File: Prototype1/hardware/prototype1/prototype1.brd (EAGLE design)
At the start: 134.6 x 74.6 mm, 83 parts, among them IC1 ICE40UL1K-CM36AITR1K, IC2 LDL112D33R, IC3 FT2232HL-REEL, IC4 93LC46BT-I_OT, IC5 M95010-WMN6P, U2 ESP-WROOM-32

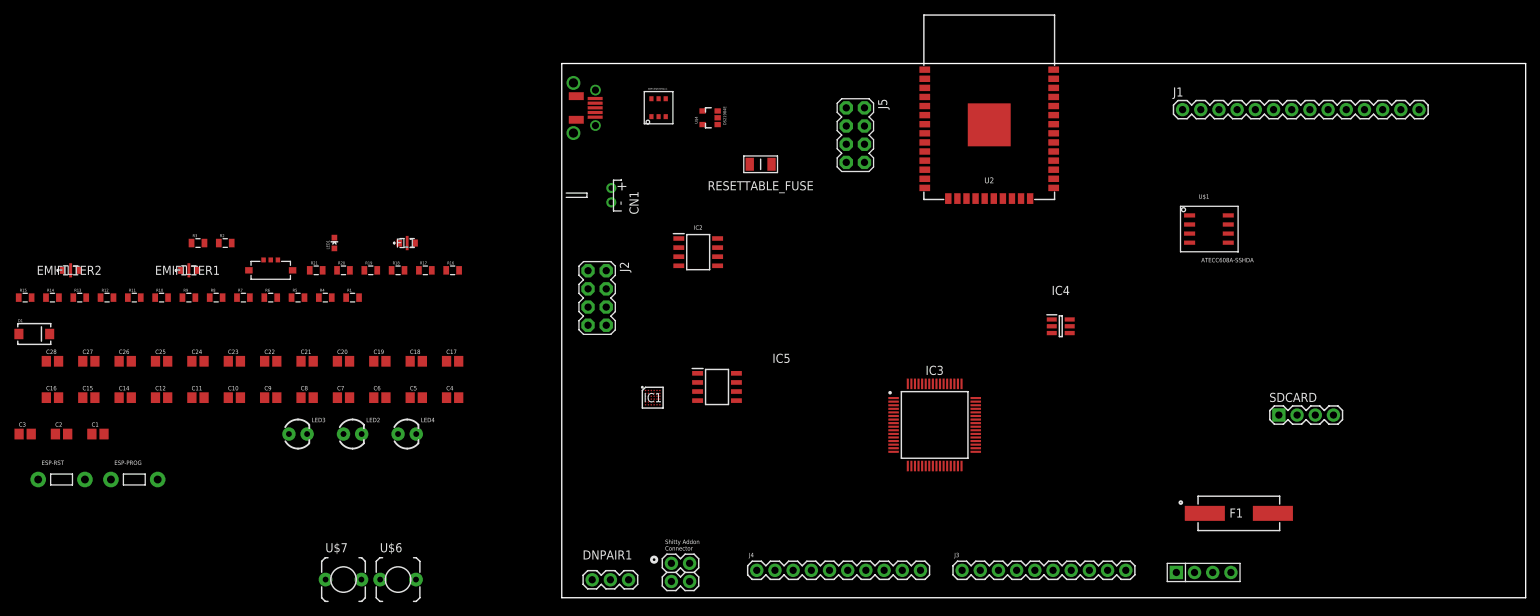
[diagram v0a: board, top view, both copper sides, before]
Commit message: initial prototype board design complete will use this one on bantam
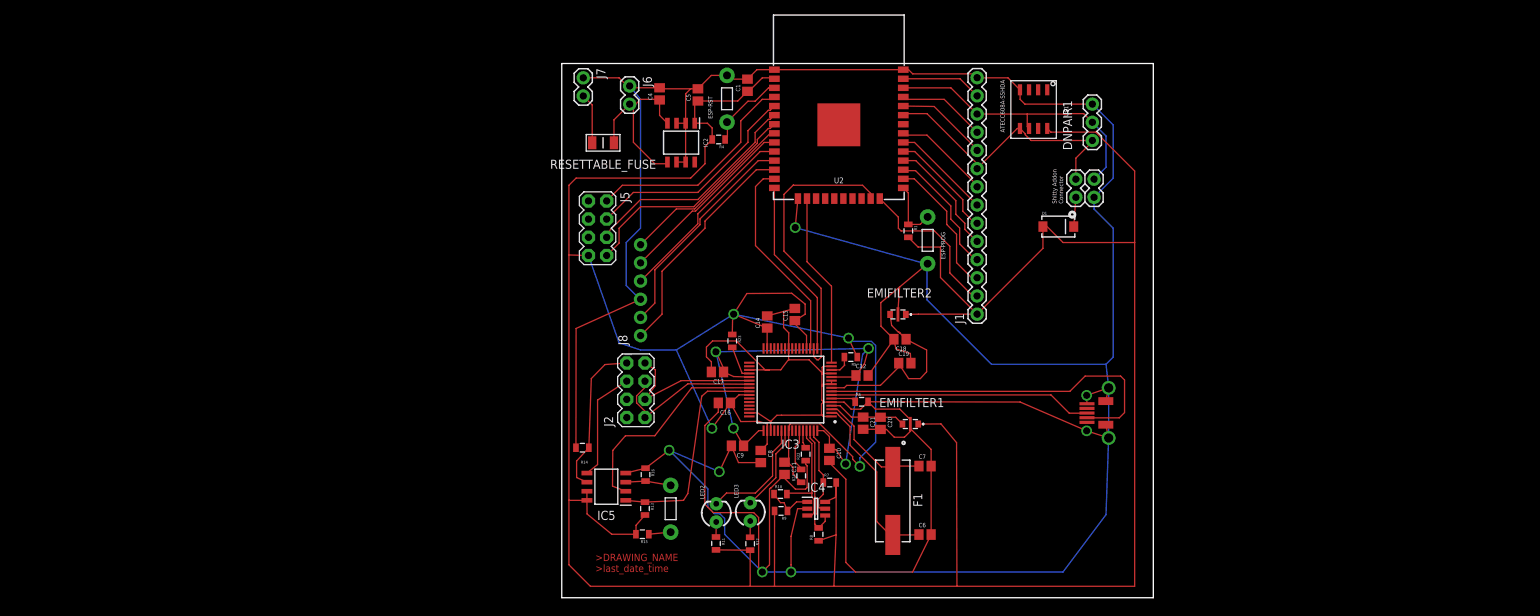
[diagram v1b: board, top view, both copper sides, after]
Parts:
- removed C2, C3: 4.7 uF, passives:C0805
- removed C22, C23, C24, C25, C28: 0.1 uf, passives:C0805
- removed C26, C27: 10 uf, passives:C0805
- removed CN1: (no value), connector:JST-PH-2-THM-RA
- removed FL1: MEM2012S101RT, passives:MEM2012S101RT
- removed IC1: ICE40UL1K-CM36AITR1K, FPGA:BGA36C40P6X6_250X250X91
- removed J3, J4: (no value), connector:1X10
- removed LED1: charging, leds:LED-0603
- removed LED4: fpga-prog-done, leds:LED3MM
- removed PROGRAMMER: SERIAL_4, connector:SERIAL_HEADER_4
- removed R17: 10 K, passives:0805
- removed R18, R20: 100, passives:0805
- removed R19, R21: 56, passives:0805
- removed R2, R3: (no value), passives:0805
- removed SDCARD: (no value), connector:1X04
- removed U$3: XBP15SRV05W-G, passives:SOT-26P-XBP15SRV05W-G
- removed U$4: DS21984E, charging-ic:SOT23-5
- removed U$5: SWITCH_SPDT, switches:SPDT_SSAJ120100
- removed U$6: SWITCH_TACTILETACTILE-2PIN, switches:TACTILE-2PIN
- added J6: (no value), connector:1X02
- added J7: TMP BATTERY, connector:1X02
- added J8: (no value), connector:1X06_NO_SILK_YES_STOP
- added R22: 4.7K, passives:0805
- added R23, R24: 10 K, passives:0805
- R6: value 12 K -> 10 K
- U$7: value SWITCH_TACTILETACTILE-2PIN -> SWITCH_TACTILETACTILE-2PIN-NARROW; device switches:TACTILE-2PIN -> switches:TACTILE-2PIN-NARROW
- moved D1 143.8 mm to (69.3, 77.2)
- moved ESP-PROG 115.7 mm to (51.1, 75.3), turned to 90 degrees
- moved EMIFILTER2 115.7 mm to (46.9, 65.0), turned to 180 degrees
- moved ESP-RST 107.1 mm to (23.1, 95.1), turned to 90 degrees
- moved EMIFILTER1 103.0 mm to (48.7, 49.7), turned to 180 degrees
- moved C1 103.0 mm to (25.9, 97.0), turned to 90 degrees
- moved C15 99.3 mm to (32.5, 64.9), turned to 90 degrees
- moved C12 97.9 mm to (41.9, 56.4)
- moved R12 96.2 mm to (26.3, 32.9), turned to 270 degrees
- moved C16 93.8 mm to (22.7, 52.6), turned to 180 degrees
- moved DNPAIR1 93.0 mm to (74.1, 89.2), turned to 90 degrees
- moved R15 92.3 mm to (11.3, 34.3), turned to 180 degrees
- moved R10 90.7 mm to (30.5, 39.9)
- moved R8 90.4 mm to (35.9, 34.3), turned to 90 degrees
- moved C14 90.3 mm to (28.7, 63.9), turned to 90 degrees
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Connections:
- removed net BARCODE: IC1.A5, J3.7
- removed net CRESET_B: IC1.F4, R17.1, U$6.P$2
- removed net IOB0A: IC1.F1, J4.3
- removed net IOB10A: IC1.D6, J4.6
- removed net IOB3BG6: IC1.F2, J4.2
- removed net IOB4A: IC1.D1, J4.8
- removed net IOB5B: IC1.C1, J3.1
- removed net IOB6A: IC1.E2, J4.4
- removed net IOB7BG5: IC1.F3, J4.1
- removed net IOB8AG4: IC1.D2, J4.7
- removed net IOB_1B: IC1.E1, J4.5
- removed net IOT12AG1: IC1.B6, J3.2
- removed net IOT18B: IC1.B5, J3.3
- removed net IOT19A: IC1.A4, J3.8
- removed net IOT22BG0: IC1.C6, J4.9
- removed net IOT24B: IC1.B2, J3.4
- removed net IOT27A: IC1.C2, J4.10
- removed net IRLED: IC1.A6, J3.6
- removed net N$1: LED1.A, R2.1
- removed net N$10: LED4.A, R21.2
- removed net N$15: FL1.3, R18.2, R19.1
- removed net N$16: FL1.1, R20.1
- removed net N$17: IC1.D5, R21.1
- removed net N$2: LED1.C, U$4.1
- removed net N$4: R3.2, U$4.5
- removed net N$5: C4.1, IC2.4, RESETTABLE_FUSE.2, U$5.2
- removed net RBG1: IC1.B1, J3.5
- removed net RBO0: IC1.A2, J3.9
- removed net RGB2: IC1.A1, J3.10
- removed net VCC-FPGA-PLL: C27.1, C28.1, IC1.D3, IC1.D4, R20.2
- removed net VCC5: C2.1, R2.2, U$2.+5V, U$4.4
- new net PWREN: IC3.60, R22.2
- new net PWRSAV: IC3.59, R24.2
- new net SUSPEND: IC3.36, R23.2
- net DISPLAY_BACKLIT: now also J1.4; no longer J1.8
- net DISPLAY_CS: now also J1.5; no longer J1.3
- net DISPLAY_DATA_CMD: now also J1.3; no longer J1.5
- net DISPLAY_RESET: now also J1.2; no longer J1.4
- net DISPLAY_SD_MISO: now also J1.8; no longer J1.9, SDCARD.3
- net DISPLAY_SD_MOSI: now also J1.13; no longer J1.6, SDCARD.2
- net DISPLAY_SD_SCK: no longer SDCARD.4
- net GND: now also J1.14, J6.1, J7.1, J8.3, R22.1; no longer C2.2, C22.2, C23.2, C24.2, C25.2, C26.1, C27.2, C28.2, C3.2, CN1.1, FL1.2, FL1.4, IC1.C3, IC1.C4, IC1.C5, J1.2, LED4.K, PROGRAMMER.GND, R19.2, R3.1, U$3.P2, U$4.2, U$5.1, U$6.P$1
- net N$12: now also C4.1, IC2.4, J6.2, RESETTABLE_FUSE.2; no longer U$5.C
- net PROG_RX: now also J1.10; no longer J2.4, PROGRAMMER.TX
- net PROG_TX: now also J1.11; no longer J2.2, PROGRAMMER.RX
- net SCL: now also J1.12
- net SDA: now also J1.9
- net SD_CS: now also J1.6; no longer SDCARD.1
- net SPI_PROM_CLK: no longer IC1.E6
- net SPI_PROM_CS: no longer IC1.F5
- net SPI_PROM_MISO: no longer IC1.F6
- net SPI_PROM_MOSI: no longer IC1.E5
- net TOUCH_CLK: now also J8.2; no longer J1.10
- net TOUCH_CS: now also J8.1; no longer J1.11
- net TOUCH_DATA_IN: now also J8.4; no longer J1.12
- net TOUCH_DATA_OUT: now also J8.5; no longer J1.13
- net TOUCH_IRQ: now also J8.6; no longer J1.14
- net USB_DM: no longer U$3.P6
- net USB_DP: no longer U$3.P1
- net VBAT: now also J7.2; no longer C3.1, CN1.2, U$4.3
- net VCC: now also J5.7, R23.1, R24.1; no longer C22.1, C23.1, C24.1, C25.1, C26.2, IC1.B3, IC1.E3, IC1.E4, PROGRAMMER.VCC, R17.2, R18.1
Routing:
- net GND: track 0.00 -> 634.8 mm, vias 0 -> 5
- net VCC: track 0.00 -> 548.7 mm, vias 0 -> 4
- net VCC1.8: track 0.00 -> 77.2 mm, vias 0 -> 4
- net USB_DP: track 0.00 -> 52.1 mm
- net JTAG_TDO: track 0.00 -> 41.2 mm
- net SCL: track 0.00 -> 40.0 mm
- net SDA: track 0.00 -> 39.5 mm
- net USB_DM: track 0.00 -> 36.7 mm
- net IO35: track 0.00 -> 32.5 mm
- net TOUCH_CS: track 0.00 -> 32.4 mm
- net IO34: track 0.00 -> 31.6 mm
- net SENSORVP: track 0.00 -> 31.2 mm
- net TOUCH_CLK: track 0.00 -> 31.0 mm
- net SENSORVN: track 0.00 -> 30.9 mm
- net SPI_PROM_MISO: track 0.00 -> 30.3 mm
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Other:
- board size 134.6 x 74.6 mm -> 82.6 x 74.6 mm
- board text added: ">DRAWING_NAME >last_date_time"

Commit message: updated breakout board
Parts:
- added U$3: CMD_C0DE_LOGOCMD_CODE_LOGO_TOP_COPPER, logos:CMD_C0DE_LOGO_TOP_COPPER
- moved R4 1.42 mm to (20.6, 89.9)
- moved IC2 1.11 mm to (15.7, 89.4)
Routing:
- net TOUCH_DATA_OUT: track 25.7 -> 32.3 mm, vias 0 -> 1
- net TOUCH_DATA_IN: track 27.0 -> 31.8 mm
- net TOUCH_CLK: track 31.0 -> 34.7 mm
- net TOUCH_CS: track 32.4 -> 35.6 mm
- net N$12: track 26.1 -> 24.2 mm
- net VCC: track 548.7 -> 546.8 mm
- net JTAG_TMS: track 28.9 -> 27.3 mm
- net SENSORVP: track 31.2 -> 30.2 mm
- net SENSORVN: track 30.9 -> 30.0 mm
- net IO35: track 32.5 -> 31.7 mm
- net IO34: track 31.6 -> 30.8 mm
- net GND: track 634.8 -> 634.2 mm
- net DISPLAY_DATA_CMD: track 19.4 -> 18.9 mm

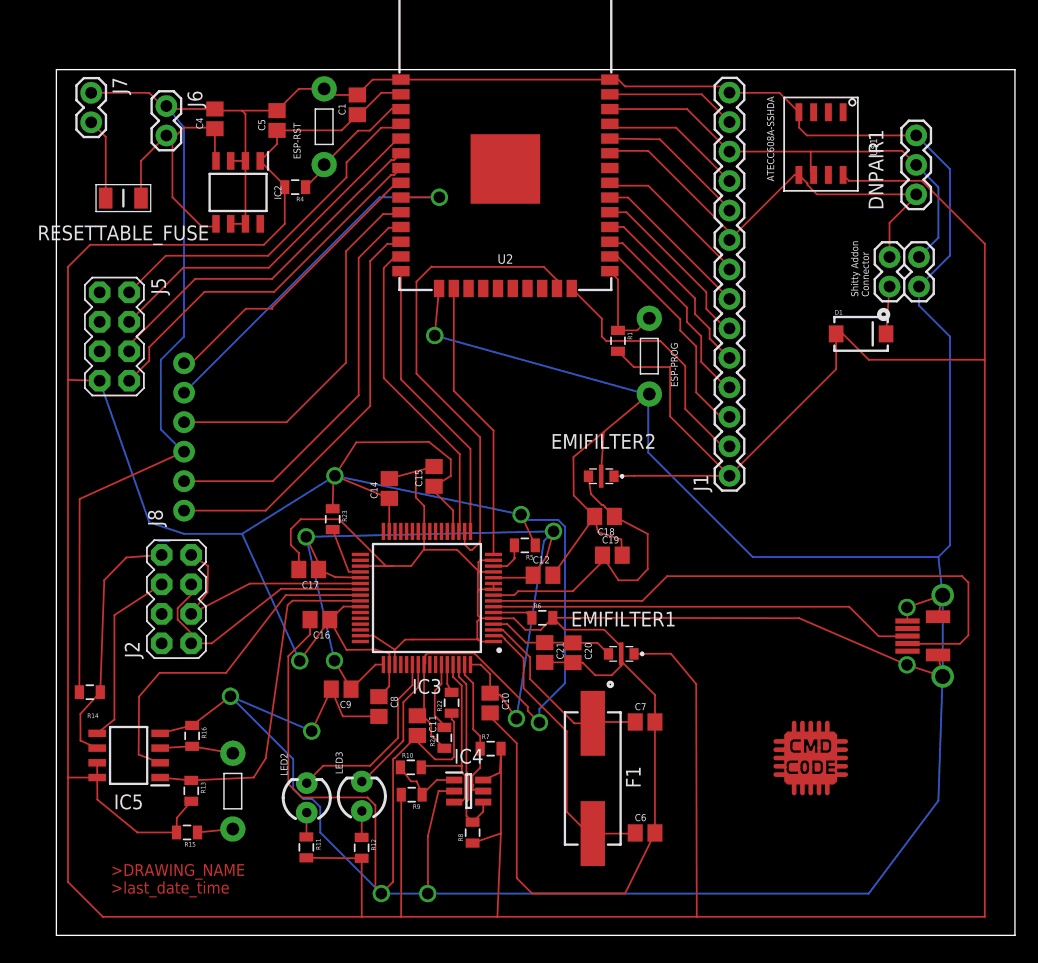
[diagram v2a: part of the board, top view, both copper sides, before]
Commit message: a bit more room between traces
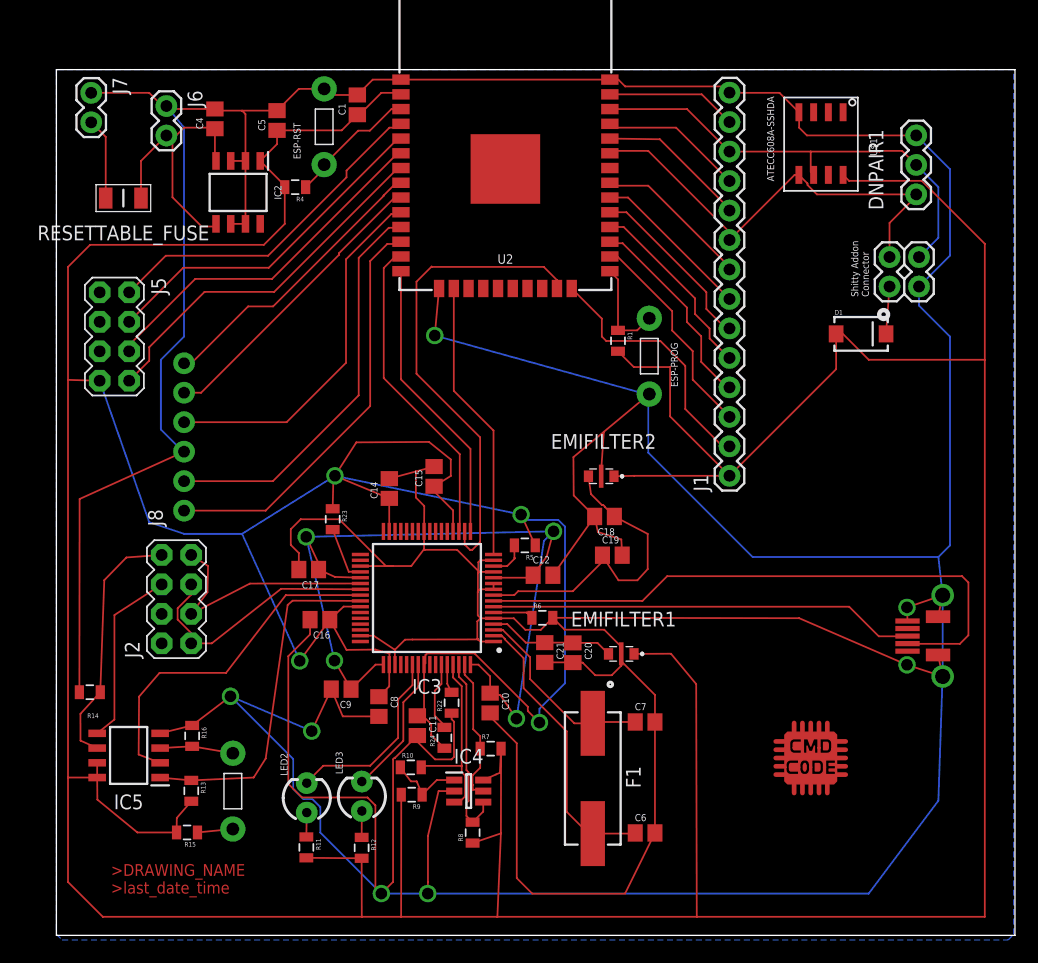
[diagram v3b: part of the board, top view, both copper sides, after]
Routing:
- net TOUCH_DATA_OUT: track 32.3 -> 25.7 mm, vias 1 -> 0
- net PROG_TX: track 13.3 -> 12.4 mm
- added copper zone on layer 16, net GND

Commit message: adding docs
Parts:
- added C2, C3: 0.1 uF, passives:C0805
- C6, C7: value 20 pF -> 27 pF
- moved R4 0.30 mm to (20.9, 89.9), turned to 90 degrees
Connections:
- net GND: now also C2.1, C3.2
- net VCC: now also C2.2, C3.1
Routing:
- net VCC: track 546.8 -> 559.6 mm, vias 4 -> 5
- net GND: track 634.2 -> 642.5 mm
- net ESP-EN: track 11.3 -> 12.7 mm
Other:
- board text removed: ">DRAWING_NAME >last_date_time"
